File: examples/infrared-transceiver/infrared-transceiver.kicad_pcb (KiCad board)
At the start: 2 copper layers, 16.1 x 15.7 mm, 10 parts

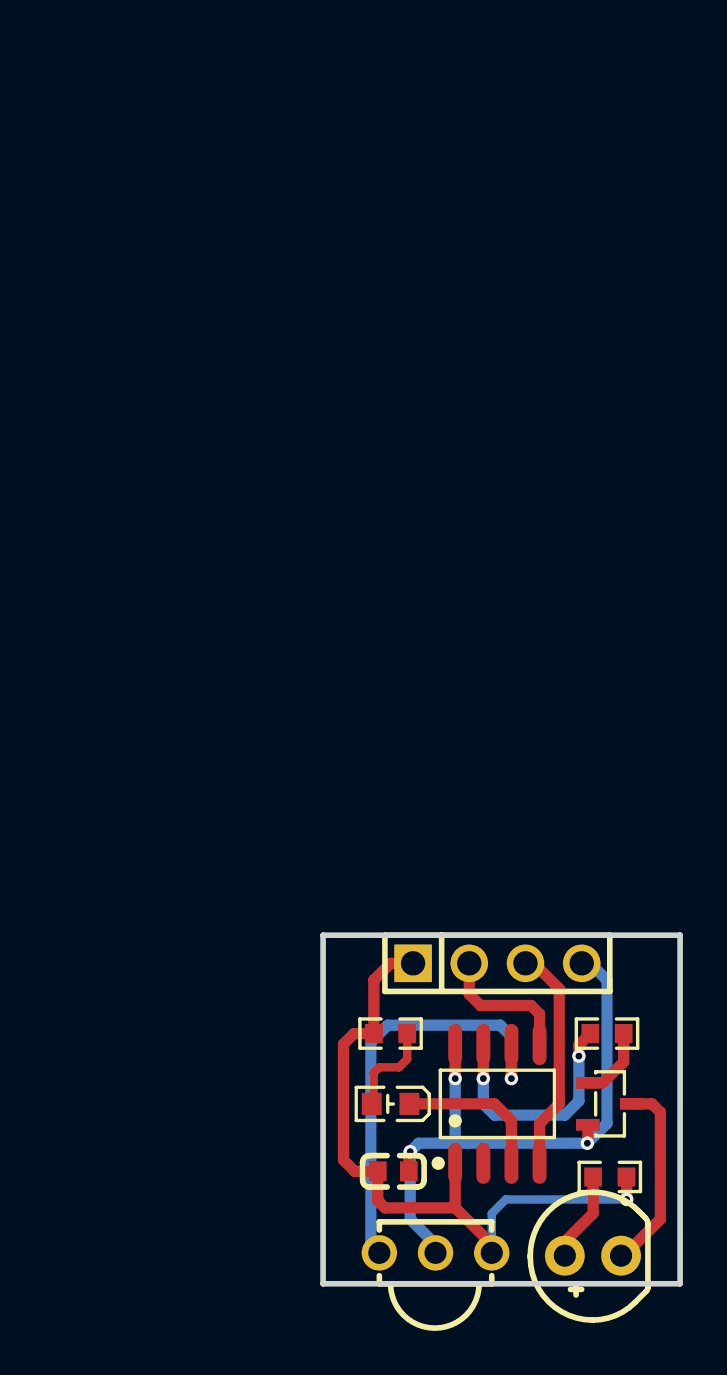
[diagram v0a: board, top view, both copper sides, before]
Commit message: fix: support hierarchical KiCad net names
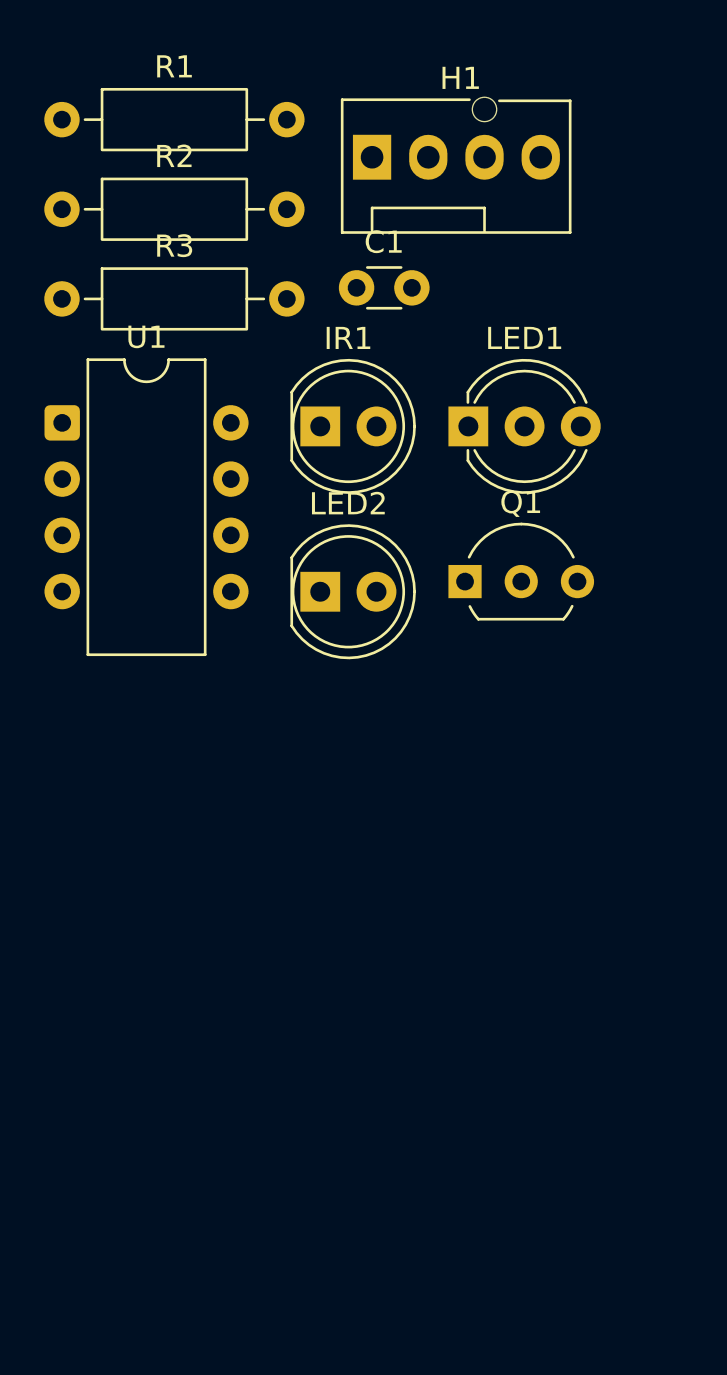
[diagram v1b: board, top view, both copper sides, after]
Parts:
- C1: value (none) -> 1uF; footprint infrared-transceiver-easyedapro:C0603 -> Capacitor_THT:C_Disc_D3.0mm_W1.6mm_P2.50mm
- H1: value (none) -> PZ254V-11-04P; footprint infrared-transceiver-easyedapro:HDR-TH_4P-P2.54-V-M -> Connector:FanPinHeader_1x04_P2.54mm_Vertical
- IR1: value (none) -> IR333C-A; footprint infrared-transceiver-easyedapro:LED-TH_BD5.9-P2.54-RD_WHITE -> LED_THT:LED_D5.0mm
- LED1: value (none) -> TSOP38238; footprint infrared-transceiver-easyedapro:SENSOR-TG_TSOP38236 -> LED_THT:LED_D5.0mm-3
- LED2: value (none) -> GL0603UR01; footprint infrared-transceiver-easyedapro:LED0603-FD -> LED_THT:LED_D5.0mm
- Q1: value (none) -> S8050; footprint infrared-transceiver-easyedapro:SOT-23-3_L2.9-W1.3-P1.90-LS2.3-BR -> Package_TO_SOT_THT:TO-92L_Inline_Wide
- R1, R2: value (none) -> 510Ω; footprint infrared-transceiver-easyedapro:R0603 -> Resistor_THT:R_Axial_DIN0207_L6.3mm_D2.5mm_P10.16mm_Horizontal
- R3: value (none) -> 1kΩ; footprint infrared-transceiver-easyedapro:R0603 -> Resistor_THT:R_Axial_DIN0207_L6.3mm_D2.5mm_P10.16mm_Horizontal
- U1: value (none) -> TXMCU; footprint infrared-transceiver-easyedapro:SOP-8_L4.9-W3.9-P1.27-LS6.0-BL-1 -> Package_DIP:CERDIP-8_W7.62mm_SideBrazed
- moved R2 50.2 mm to (130.1, 69.1)
- moved R1 43.9 mm to (130.1, 65.0), turned to 0 degrees
- moved R3 41.3 mm to (130.1, 73.1)
- moved C1 39.9 mm to (143.4, 72.6)
- moved IR1 39.4 mm to (141.7, 78.9), turned to 0 degrees
- moved LED1 37.4 mm to (148.4, 78.9)
- moved H1 36.9 mm to (144.1, 66.7)
- moved U1 36.5 mm to (130.1, 78.7)
- moved Q1 24.5 mm to (148.3, 85.9), turned to 0 degrees
- moved LED2 23.4 mm to (141.7, 86.4)
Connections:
- net $1N18 renamed Net-(LED1-OUT)
- net $1N27 renamed Net-(Q1-B)
- net $1N28 renamed Net-(U1-IO7)
- net $1N29 renamed Net-(IR1-C)
- net $1N30 renamed Net-(IR1-A)
- net $1N32 renamed Net-(LED2-A)
- net $1N35 renamed Net-(LED2-C)
- net RX renamed /RX
- net TX renamed /TX
- U1 pad 2: (no net) -> unconnected-(U1-IO2-Pad2)
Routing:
- net VCC: track 31.9 -> 0.00 mm, vias 1 -> 0
- net GND: track 28.6 -> 0.00 mm, vias 3 -> 0
- net Net-(LED1-OUT): track 20.0 -> 0.00 mm, vias 1 -> 0
- net Net-(U1-IO7): track 10.7 -> 0.00 mm, vias 2 -> 0
- net /TX: track 10.4 -> 0.00 mm
- net Net-(IR1-C): track 8.74 -> 0.00 mm
- net Net-(LED2-C): track 6.85 -> 0.00 mm
- net /RX: track 6.70 -> 0.00 mm
- net Net-(LED2-A): track 4.36 -> 0.00 mm
- net Net-(IR1-A): track 4.09 -> 0.00 mm
- net Net-(Q1-B): track 3.29 -> 0.00 mm
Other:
- board outline removed
- board text removed: "GND"
- board text removed: "REC"
- board text removed: "RXD"
- board text removed: "TXD"
- board text removed: "VCC"
